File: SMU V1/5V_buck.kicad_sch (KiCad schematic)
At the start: 15 parts, among them U1001 TPS5430DDAR, U1002 ETQ-P3M150KVN

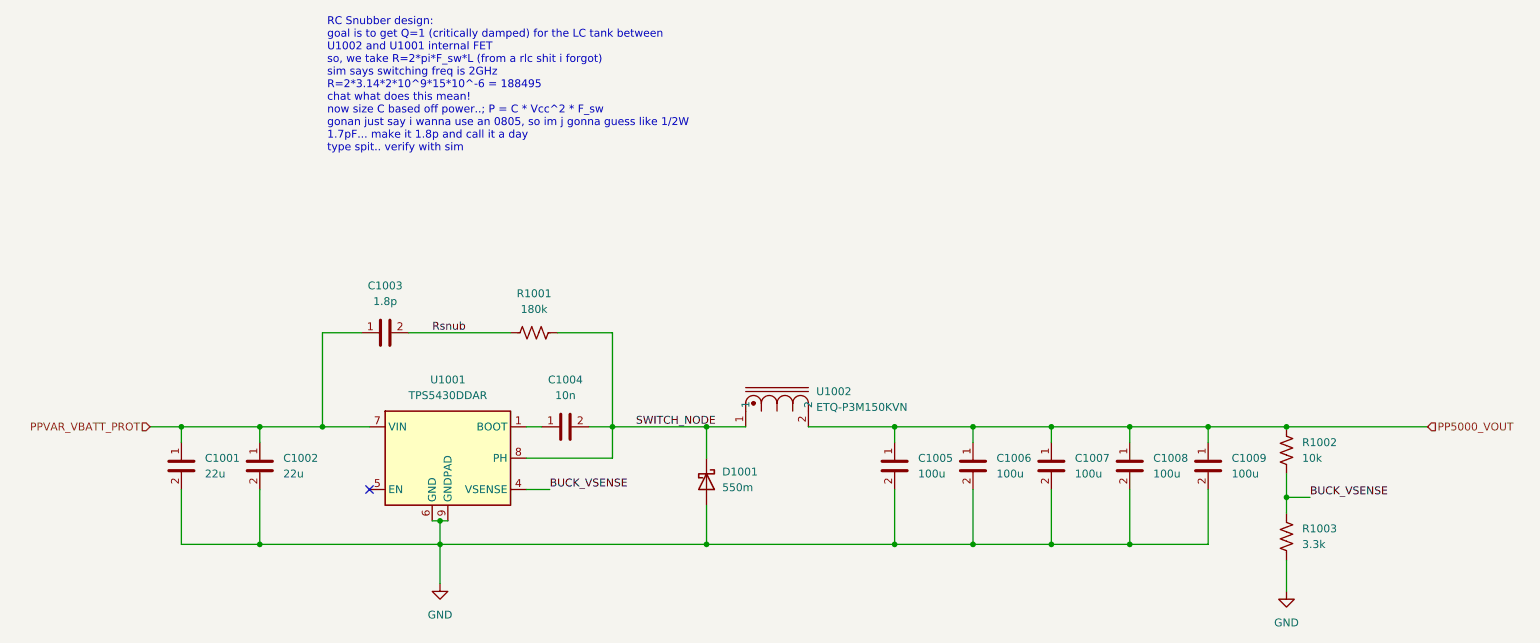
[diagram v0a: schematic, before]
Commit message: halfway done with routing, still needs antenna
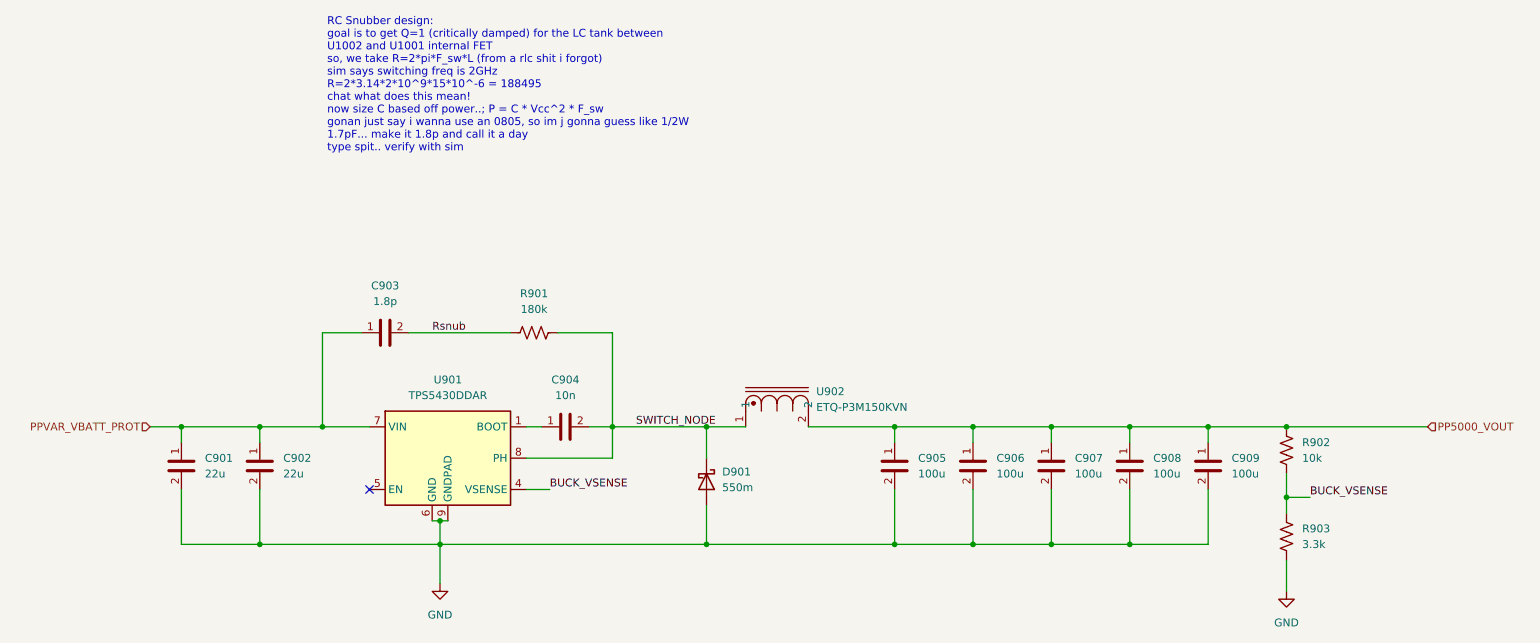
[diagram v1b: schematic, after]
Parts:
- U901: renamed from U1001; footprint Package_SO:TI_SO-PowerPAD-8_ThermalVias -> Package_SO:TI_SO-PowerPAD-8
- U902: renamed from U1002; footprint (none) -> bfr_inductors:BWVS005050404R7M00
- renumbered C1001 to C901, C1002 to C902, C1003 to C903, C1004 to C904, C1005 to C905, C1006 to C906, C1007 to C907, C1008 to C908, C1009 to C909, D1001 to D901, R1001 to R901, R1002 to R902, R1003 to R903
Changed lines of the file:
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@@
 		(dnp no)
 		(fields_autoplaced yes)
-		(property "Reference" "U1002"
+		(property "Reference" "U902"
 			(at 153.67 76.8349 90)
 			(effects
@@
 			)
 		)
-		(property "Footprint" ""
+		(property "Footprint" "bfr_inductors:BWVS005050404R7M00"
 			(at 153.67 82.55 0)
 			(effects
@@
 		)
 		(property "Created By" "Tony"
+			(at 153.67 82.55 0)
+			(effects
+				(font
+					(size 1.27 1.27)
+				)
+				(hide yes)
+			)
+		)
+		(property "Pretty Name" ""
 			(at 153.67 82.55 0)
 			(effects
@@
 			(project "SMU V1"
 				(path "/1f58b889-96e6-4877-90a3-5a655db5910b/b9f10619-4e5b-45af-b866-c6815d605ed5/af802241-6422-4666-a084-41c36db8cc4c"
-					(reference "U1002")
+					(reference "U902")
 					(unit 1)
 				)
@@
 		(dnp no)
 		(fields_autoplaced yes)
-		(property "Reference" "C1004"
+		(property "Reference" "C904"
 			(at 113.03 74.93 90)
 			(effects
@@
 			(project "SMU V1"
 				(path "/1f58b889-96e6-4877-90a3-5a655db5910b/b9f10619-4e5b-45af-b866-c6815d605ed5/af802241-6422-4666-a084-41c36db8cc4c"
-					(reference "C1004")
+					(reference "C904")
 					(unit 1)
 				)
@@
 		(dnp no)
 		(fields_autoplaced yes)
-		(property "Reference" "#PWR01002"
+		(property "Reference" "#PWR0902"
 			(at 229.87 115.57 0)
 			(effects
@@
 			(project "SMU V1"
 				(path "/1f58b889-96e6-4877-90a3-5a655db5910b/b9f10619-4e5b-45af-b866-c6815d605ed5/af802241-6422-4666-a084-41c36db8cc4c"
-					(reference "#PWR01002")
+					(reference "#PWR0902")
 					(unit 1)
 				)
@@
 		(dnp no)
 		(fields_autoplaced yes)
-		(property "Reference" "C1003"
+		(property "Reference" "C903"
 			(at 83.82 59.69 90)
 			(effects
@@
 			(project ""
 				(path "/1f58b889-96e6-4877-90a3-5a655db5910b/b9f10619-4e5b-45af-b866-c6815d605ed5/af802241-6422-4666-a084-41c36db8cc4c"
-					(reference "C1003")
+					(reference "C903")
 					(unit 1)
 				)
@@
 		(dnp no)
 		(fields_autoplaced yes)
-		(property "Reference" "C1009"
+		(property "Reference" "C909"
 			(at 220.98 87.6299 0)
 			(effects
@@
 			(project "SMU V1"
 				(path "/1f58b889-96e6-4877-90a3-5a655db5910b/b9f10619-4e5b-45af-b866-c6815d605ed5/af802241-6422-4666-a084-41c36db8cc4c"
-					(reference "C1009")
+					(reference "C909")
 					(unit 1)
 				)
@@
 		(dnp no)
 		(fields_autoplaced yes)
-		(property "Reference" "D1001"
+		(property "Reference" "D901"
 			(at 138.43 89.8524 90)
 			(effects
@@
 			(project "SMU V1"
 				(path "/1f58b889-96e6-4877-90a3-5a655db5910b/b9f10619-4e5b-45af-b866-c6815d605ed5/af802241-6422-4666-a084-41c36db8cc4c"
-					(reference "D1001")
+					(reference "D901")
 					(unit 1)
 				)
@@
 		(dnp no)
 		(fields_autoplaced yes)
-		(property "Reference" "R1002"
+		(property "Reference" "R902"
 			(at 232.41 85.0899 90)
 			(effects
@@
 			(project "SMU V1"
 				(path "/1f58b889-96e6-4877-90a3-5a655db5910b/b9f10619-4e5b-45af-b866-c6815d605ed5/af802241-6422-4666-a084-41c36db8cc4c"
-					(reference "R1002")
+					(reference "R902")
 					(unit 1)
 				)
@@
 		(dnp no)
 		(fields_autoplaced yes)
-		(property "Reference" "U1001"
+		(property "Reference" "U901"
 			(at 93.98 74.93 0)
 			(effects
@@
 			)
 		)
-		(property "Footprint" "Package_SO:TI_SO-PowerPAD-8_ThermalVias"
+		(property "Footprint" "Package_SO:TI_SO-PowerPAD-8"
 			(at 95.25 96.52 0)
 			(effects
@@
 		(property "Sim.Pins" "1=BOOT 2=NC 3=NC1 4=VSENSE 5=ENA 6=GND 7=VIN 8=PH 9=PAD"
 			(at 93.98 74.93 0)
+			(effects
+				(font
+					(size 1.27 1.27)
+				)
+				(hide yes)
+			)
+		)
+		(property "Manufacturer P/N" ""
+			(at 93.98 87.63 0)
+			(effects
+				(font
+					(size 1.27 1.27)
+				)
+				(hide yes)
+			)
+		)
+		(property "Manufacturer" ""
+			(at 93.98 87.63 0)
+			(effects
+				(font
+					(size 1.27 1.27)
+				)
+				(hide yes)
+			)
+		)
+		(property "JLC Basic Part" ""
+			(at 93.98 87.63 0)
+			(effects
+				(font
+					(size 1.27 1.27)
+				)
+				(hide yes)
+			)
+		)
+		(property "Created By" ""
+			(at 93.98 87.63 0)
 			(effects
 				(font
@@
 			(project "SMU V1"
 				(path "/1f58b889-96e6-4877-90a3-5a655db5910b/b9f10619-4e5b-45af-b866-c6815d605ed5/af802241-6422-4666-a084-41c36db8cc4c"
-					(reference "U1001")
+					(reference "U901")
 					(unit 1)
 				)
@@
 		(dnp no)
 		(fields_autoplaced yes)
-		(property "Reference" "C1006"
+		(property "Reference" "C906"
 			(at 182.88 87.6299 0)
 			(effects
@@
 			(project "SMU V1"
 				(path "/1f58b889-96e6-4877-90a3-5a655db5910b/b9f10619-4e5b-45af-b866-c6815d605ed5/af802241-6422-4666-a084-41c36db8cc4c"
-					(reference "C1006")
+					(reference "C906")
 					(unit 1)
 				)
@@
 		(dnp no)
 		(fields_autoplaced yes)
-		(property "Reference" "C1001"
+		(property "Reference" "C901"
 			(at 54.61 87.6299 0)
 			(effects
@@
 			(project "SMU V1"
 				(path "/1f58b889-96e6-4877-90a3-5a655db5910b/b9f10619-4e5b-45af-b866-c6815d605ed5/af802241-6422-4666-a084-41c36db8cc4c"
-					(reference "C1001")
+					(reference "C901")
 					(unit 1)
 				)
@@
 		(dnp no)
 		(fields_autoplaced yes)
-		(property "Reference" "R1003"
+		(property "Reference" "R903"
 			(at 232.41 99.0599 90)
 			(effects
@@
 			(project "SMU V1"
 				(path "/1f58b889-96e6-4877-90a3-5a655db5910b/b9f10619-4e5b-45af-b866-c6815d605ed5/af802241-6422-4666-a084-41c36db8cc4c"
-					(reference "R1003")
+					(reference "R903")
 					(unit 1)
 				)
@@
 		(dnp no)
 		(fields_autoplaced yes)
-		(property "Reference" "C1002"
+		(property "Reference" "C902"
 			(at 67.31 87.6299 0)
 			(effects
@@
 			(project "SMU V1"
 				(path "/1f58b889-96e6-4877-90a3-5a655db5910b/b9f10619-4e5b-45af-b866-c6815d605ed5/af802241-6422-4666-a084-41c36db8cc4c"
-					(reference "C1002")
+					(reference "C902")
 					(unit 1)
 				)
@@
 		(dnp no)
 		(fields_autoplaced yes)
-		(property "Reference" "C1007"
+		(property "Reference" "C907"
 			(at 195.58 87.6299 0)
 			(effects
@@
 			(project "SMU V1"
 				(path "/1f58b889-96e6-4877-90a3-5a655db5910b/b9f10619-4e5b-45af-b866-c6815d605ed5/af802241-6422-4666-a084-41c36db8cc4c"
-					(reference "C1007")
+					(reference "C907")
 					(unit 1)
 				)
@@
 		(dnp no)
 		(fields_autoplaced yes)
-		(property "Reference" "C1005"
+		(property "Reference" "C905"
 			(at 170.18 87.6299 0)
 			(effects
@@
 			(project "SMU V1"
 				(path "/1f58b889-96e6-4877-90a3-5a655db5910b/b9f10619-4e5b-45af-b866-c6815d605ed5/af802241-6422-4666-a084-41c36db8cc4c"
-					(reference "C1005")
+					(reference "C905")
 					(unit 1)
 				)
@@
 		(dnp no)
 		(fields_autoplaced yes)
-		(property "Reference" "#PWR01001"
+		(property "Reference" "#PWR0901"
 			(at 92.71 114.3 0)
 			(effects
@@
 			(project "SMU V1"
 				(path "/1f58b889-96e6-4877-90a3-5a655db5910b/b9f10619-4e5b-45af-b866-c6815d605ed5/af802241-6422-4666-a084-41c36db8cc4c"
-					(reference "#PWR01001")
+					(reference "#PWR0901")
 					(unit 1)
 				)
@@
 		(dnp no)
 		(fields_autoplaced yes)
-		(property "Reference" "R1001"
+		(property "Reference" "R901"
 			(at 107.95 60.96 0)
 			(effects
@@
 			(project ""
 				(path "/1f58b889-96e6-4877-90a3-5a655db5910b/b9f10619-4e5b-45af-b866-c6815d605ed5/af802241-6422-4666-a084-41c36db8cc4c"
-					(reference "R1001")
+					(reference "R901")
 					(unit 1)
 				)
@@
 		(dnp no)
 		(fields_autoplaced yes)
-		(property "Reference" "C1008"
+		(property "Reference" "C908"
 			(at 208.28 87.6299 0)
 			(effects
@@
 			(project "SMU V1"
 				(path "/1f58b889-96e6-4877-90a3-5a655db5910b/b9f10619-4e5b-45af-b866-c6815d605ed5/af802241-6422-4666-a084-41c36db8cc4c"
-					(reference "C1008")
+					(reference "C908")
 					(unit 1)
 				)
